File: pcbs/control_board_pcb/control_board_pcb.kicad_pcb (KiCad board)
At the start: 2 copper layers, 124.2 x 89.8 mm, 5 parts, among them U1 MT3608, U2 MT3608, U3 MT3608, U4 MT3608, U5 ESP32 WROOM 32D DevKit

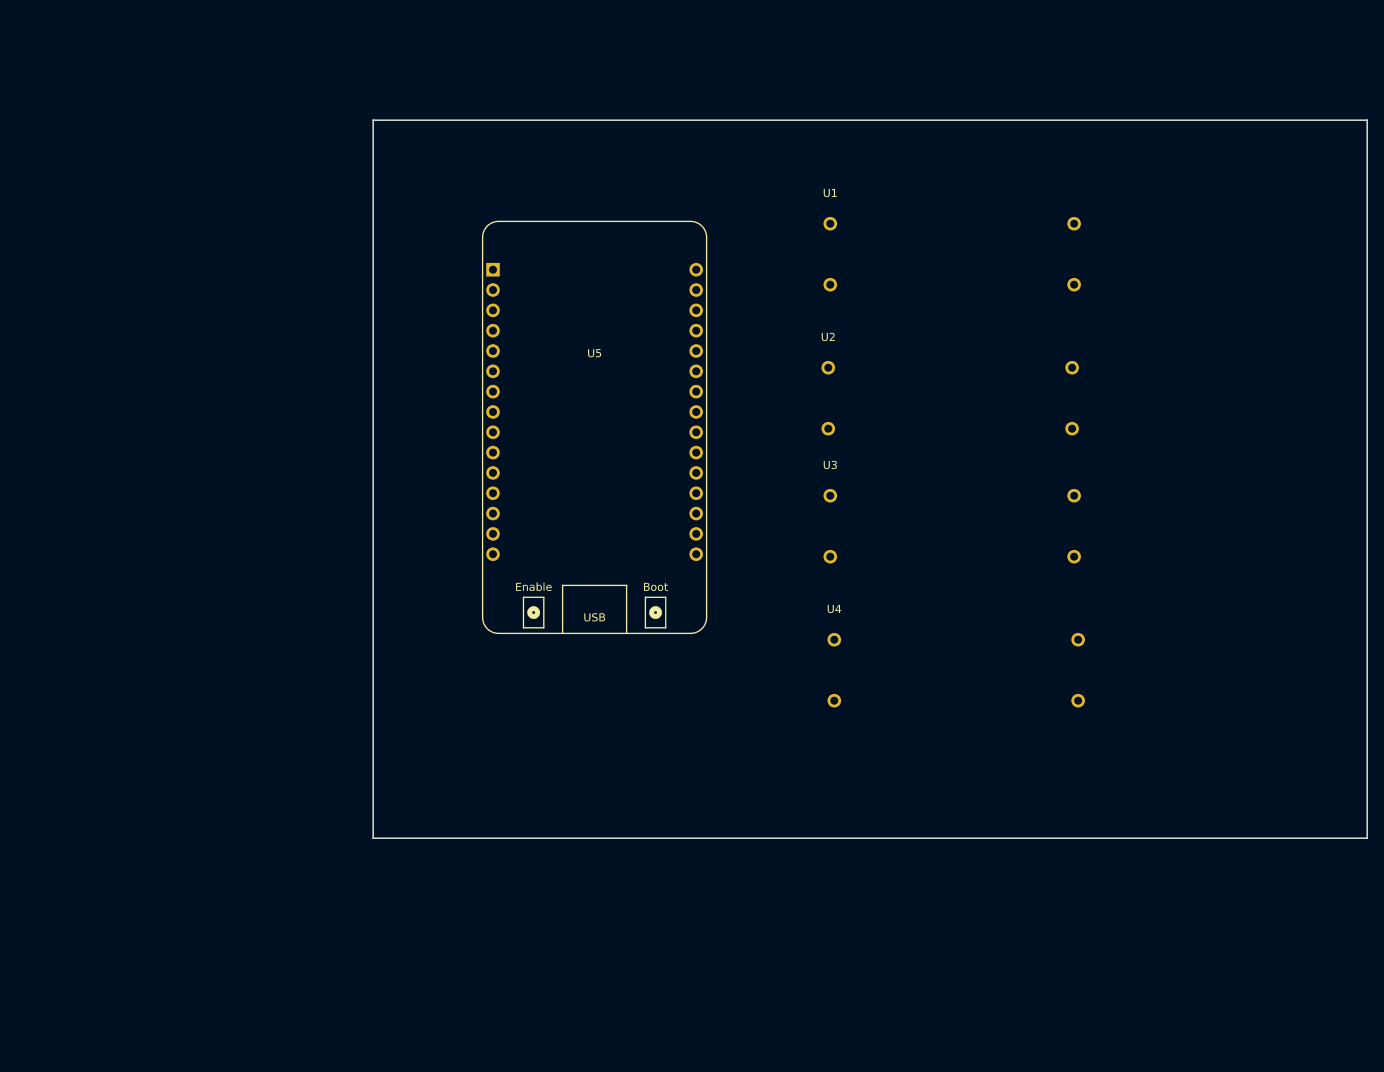
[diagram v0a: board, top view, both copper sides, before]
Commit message: Control PCB nearly complete
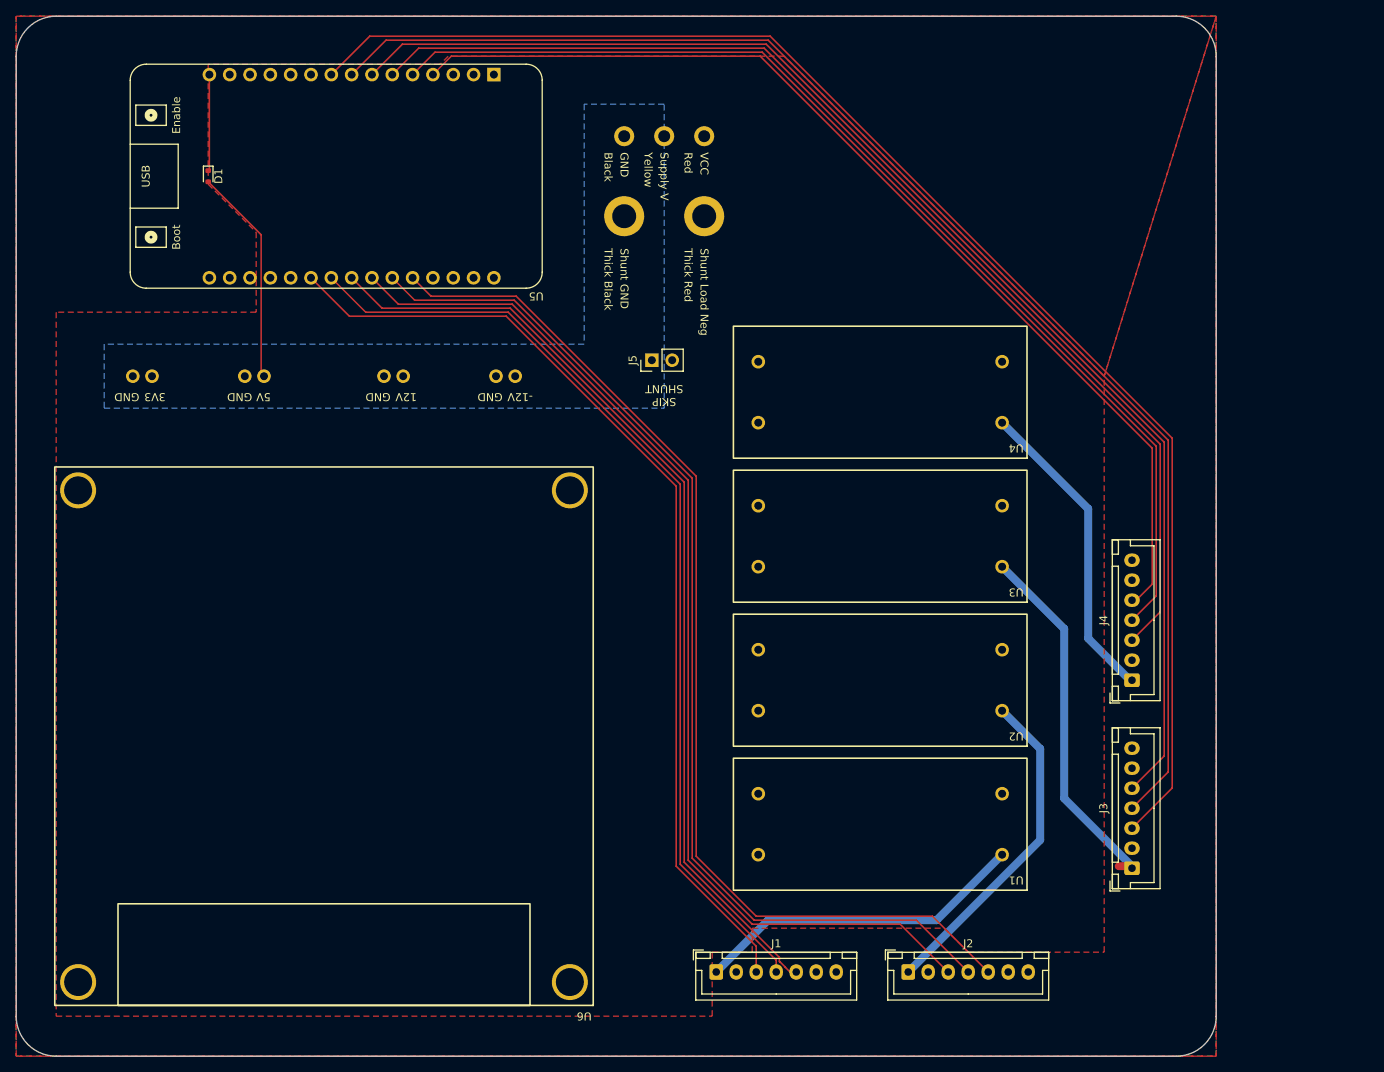
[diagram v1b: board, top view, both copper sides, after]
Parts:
- added D1: 1N4148WT, Diode_SMD:D_SOD-523, F.Cu at (59.0, 50.0)
- added J1: Conn_01x07, Connector_JST:JST_XH_B7B-XH-A_1x07_P2.50mm_Vertical, F.Cu at (122.5, 149.5)
- added J2: Conn_01x07, Connector_JST:JST_XH_B7B-XH-A_1x07_P2.50mm_Vertical, F.Cu at (146.5, 149.5)
- added J3: Conn_01x07, Connector_JST:JST_XH_B7B-XH-A_1x07_P2.50mm_Vertical, F.Cu at (174.5, 136.5)
- added J4: Conn_01x07, Connector_JST:JST_XH_B7B-XH-A_1x07_P2.50mm_Vertical, F.Cu at (174.5, 113.0)
- added J5: Conn_01x02, Connector_PinHeader_2.54mm:PinHeader_1x02_P2.54mm_Vertical, F.Cu at (114.5, 73.0)
- added U6: HU-M28, control_board_pcb:HU-M28, F.Cu at (73.5, 120.0)
- added U7: DSN-VC288, control_board_pcb:DSN-VC228_Pin-Holes, F.Cu at (116.0, 50.0)
- moved U1 71.8 mm to (143.0, 131.0), turned to 180 degrees
- moved U2 36.3 mm to (143.0, 113.0), turned to 180 degrees
- moved U4 36.0 mm to (143.0, 77.0), turned to 180 degrees
- moved U5 17.2 mm to (94.7, 50.0), turned to -90 degrees
- moved U3 9.09 mm to (143.0, 95.0), turned to 180 degrees
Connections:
- U1 pad 2: (no net) -> GND
- U1 pad 3: (no net) -> +24V_1
- U1 pad 4: (no net) -> GND
- U2 pad 2: (no net) -> GND
- U2 pad 3: (no net) -> +24V_2
- U2 pad 4: (no net) -> GND
- U3 pad 2: (no net) -> GND
- U3 pad 3: (no net) -> +24V_3
- U3 pad 4: (no net) -> GND
- U4 pad 2: (no net) -> GND
- U4 pad 3: (no net) -> +24V_4
- U4 pad 4: (no net) -> GND
- U5 pad 14: Net-(U5-GND-Pad14) -> GND
- U5 pad 15: unconnected-(U5-VIN-Pad15) -> Net-(D1-K)
- U5 pad 16: unconnected-(U5-3V3-Pad16) -> +3V3
- U5 pad 17: Net-(U5-GND-Pad14) -> GND
- U5 pad 21: unconnected-(U5-D16-Pad21) -> /STEP_1
- U5 pad 22: unconnected-(U5-D17-Pad22) -> /DIR_1
- U5 pad 23: unconnected-(U5-D5-Pad23) -> /EN_1
- U5 pad 24: unconnected-(U5-D18-Pad24) -> /STEP_2
- U5 pad 25: unconnected-(U5-D19-Pad25) -> /DIR_2
- U5 pad 26: unconnected-(U5-D21-Pad26) -> /EN_2
- U5 pad 4: unconnected-(U5-D34-Pad4) -> /EN_4
- U5 pad 5: unconnected-(U5-D35-Pad5) -> /DIR_4
- U5 pad 6: unconnected-(U5-D32-Pad6) -> /STEP_4
- U5 pad 7: unconnected-(U5-D33-Pad7) -> /EN_3
- U5 pad 8: unconnected-(U5-D25-Pad8) -> /DIR_3
- U5 pad 9: unconnected-(U5-D26-Pad9) -> /STEP_3
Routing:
- net /STEP_3: track 0.00 -> 178.7 mm
- net /DIR_3: track 0.00 -> 172.4 mm
- net /EN_3: track 0.00 -> 166.1 mm
- net /STEP_4: track 0.00 -> 143.8 mm
- net /DIR_4: track 0.00 -> 137.5 mm
- net /STEP_2: track 0.00 -> 135.8 mm
- net /DIR_2: track 0.00 -> 135.8 mm
- net /EN_2: track 0.00 -> 135.7 mm
- net /EN_4: track 0.00 -> 131.5 mm
- net /STEP_1: track 0.00 -> 121.3 mm
- net /DIR_1: track 0.00 -> 120.2 mm
- net /EN_1: track 0.00 -> 119.6 mm
- net +24V_3: track 0.00 -> 45.8 mm
- net +24V_1: track 0.00 -> 41.8 mm
- net +24V_2: track 0.00 -> 41.5 mm
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- added copper zone on F.Cu, net +12V
- added copper zone on F.Cu, net +3V3
- added copper zone on B.Cu, net GND
- added copper zone on In1.Cu, net GND
- added copper zone on In2.Cu, net GND
- added copper zone on B.Cu, net GND_PSU
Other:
- board size 124.2 x 89.8 mm -> 150 x 130 mm
- copper layers 2 -> 4
- board text added: "SKIP SHUNT"
- board text added: "U5"
